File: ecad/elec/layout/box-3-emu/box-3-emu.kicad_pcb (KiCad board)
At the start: 2 copper layers, 72.5 x 63.9 mm, 68 parts

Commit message: feat(ecad): Update ecad / atopile and improve workflow
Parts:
- removed DS1: , lib:SOD-323_L1.8-W1.3-LS2.5-RD
- removed J1: , lib:CONN-SMD_4P-P1.00_SM04B-SRSS-TB-LF-SN
- removed R27: 62.5mW Thick Film Resistors 50V ±100ppm/℃ ±1% 249Ω 0402 Chi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, lib:R0402
- removed U10: , Connector_PinHeader_1.00mm:PinHeader_1x02_P1.00mm_Vertical
- removed U11: , lib:GAMEBOY_COLOR_DPAD_MEMBRANE
- removed U12, U13, U14, U15: , lib:GBC_DPAD_BUTTON
- removed U16, U19: , lib:GAMEBOY_COLOR_A_B_BUTTON_MEMBRANE
- removed U17, U18, U20, U21: , lib:GBC_A_B_BUTTON
- removed U22: , lib:GAMEBOY_COLOR_START_SELECT_MEMBRANE
- removed U23, U24: , lib:GBC_START_SELECT_BUTTON
- removed U25, U26: , lib:SW-SMD_TS24CA
- removed U27: , lib:BOX_3_EMU
- removed U28: , lib:CONN-SMD_5-1734857-1
- removed U7: , lib:DFN-8_L2.0-W2.0-P0.50-BL-EP
- removed U8: , lib:SIM-SMD_C9900007362
- removed U9: , lib:VSSOP-10_L3.0-W3.0-P0.50-LS4.9-BL
- added C10: 22µF ±20%, Samsung_Electro_Mechanics_CL21A226MAQNNNE:C0805, F.Cu at (343.7, -323.6)
- added C11: 22µF ±20%, Samsung_Electro_Mechanics_CL21A226MAQNNNE:C0805, F.Cu at (343.7, -333.6)
- added C12: 100nF ±10%, Samsung_Electro_Mechanics_CL05B104KO5NNNC:C0402, F.Cu at (343.7, -363.6)
- added C13: 100nF ±10%, Samsung_Electro_Mechanics_CL05B104KO5NNNC:C0402, F.Cu at (343.7, -373.6)
- added CN1: , JST_Sales_America_S2B_PH_SM4_TB_LF__SN:CONN-SMD_P2.00_S2B-PH-SM4-TB-LF-SN, B.Cu at (32.4, 24.6)
- added CN2: , JST_Sales_America_SM04B_SRSS_TB_LF__SN:CONN-SMD_4P-P1.00_SM04B-SRSS-TB-LF-SN, F.Cu at (73.7, -33.6)
- added CN3: , TE_Connectivity_5_1734857_1:CONN-SMD_5-1734857-1, F.Cu at (310.0, 0.00)
- added D1: , Guangdong_Hottech_1N5819WS:SOD-323_L1.8-W1.3-LS2.5-RD, F.Cu at (29.6, 17.7)
- added H1: , Ckmtw_B_2100S02P_A110:HDR-TH_2P-P2.54-V-M-1, F.Cu at (44.8, -31.2)
- added MECH1: , GBC_A_B_MEMBRANE:GAMEBOY_COLOR_A_B_BUTTON_MEMBRANE, F.Cu at (64.8, -4.19)
- added MECH2: , GBC_A_B_MEMBRANE:GAMEBOY_COLOR_A_B_BUTTON_MEMBRANE, F.Cu at (59.6, -19.4)
- added MECH3: , GBC_DPAD_MEMBRANE:GAMEBOY_COLOR_DPAD_MEMBRANE, F.Cu at (20.8, -11.8)
- added MECH4: , BOX_EMU_BASE_OUTLINE:BOX_EMU_BASE, F.Cu at (43.7, -33.6)
- added MECH5: , GBC_START_SELECT_MEMBRANE:GAMEBOY_COLOR_START_SELECT_MEMBRANE, F.Cu at (42.2, 10.4)
- added MECH6: , BOX_3_EMU_OUTLINE:BOX_3_EMU, F.Cu at (309.7, -1.05)
- added SW1: , GBC_A_B_BUTTON:GBC_A_B_BUTTON, F.Cu at (71.8, -6.60)
- added SW10: , GBC_START_SELECT_BUTTON:GBC_START_SELECT_BUTTON, F.Cu at (48.4, 10.4)
- added SW11: , SHOU_HAN_TS24CA:SW-SMD_2P-TS24CA, F.Cu at (21.9, 29.1)
- added SW12: , SHOU_HAN_TS24CA:SW-SMD_2P-TS24CA, F.Cu at (27.9, 30.0)
- added SW2: , GBC_A_B_BUTTON:GBC_A_B_BUTTON, F.Cu at (57.9, -1.63)
- added SW3: , GBC_A_B_BUTTON:GBC_A_B_BUTTON, F.Cu at (66.6, -21.9)
- added SW4: , GBC_A_B_BUTTON:GBC_A_B_BUTTON, F.Cu at (52.7, -17.0)
- added SW5: , GBC_DPAD_BUTTON:GBC_DPAD_BUTTON, F.Cu at (20.8, -3.81)
- added SW6: , GBC_DPAD_BUTTON:GBC_DPAD_BUTTON, F.Cu at (12.8, -11.7)
- added SW7: , GBC_DPAD_BUTTON:GBC_DPAD_BUTTON, F.Cu at (28.8, -11.7)
- added SW8: , GBC_DPAD_BUTTON:GBC_DPAD_BUTTON, F.Cu at (20.8, -19.7)
- added SW9: , GBC_START_SELECT_BUTTON:GBC_START_SELECT_BUTTON, F.Cu at (36.8, 10.4)
- added USB1: , Yuandi_TYPE_611_T3_W:USB-C-SMD_TYPE-611-T3-W, F.Cu at (42.5, 30.3)
- C1: value 16V 100nF X7R ±10% 0402 Multilayer Ceramic Capacitors MLCC - SMD/SMT ROHS -> 100nF ±10%; footprint lib:C0402 -> Samsung_Electro_Mechanics_CL05B104KO5NNNC:C0402
- C2: value 25V 10uF X5R ±10% 0805 Multilayer Ceramic Capacitors MLCC - SMD/SMT ROHS -> 1µF ±10%; footprint lib:C0805 -> Samsung_Electro_Mechanics_CL05A105KA5NQNC:C0402
- C3, C4, C5: value 25V 10uF X5R ±10% 0805 Multilayer Ceramic Capacitors MLCC - SMD/SMT ROHS -> 100nF ±10%; footprint lib:C0805 -> Samsung_Electro_Mechanics_CL05B104KO5NNNC:C0402
- C6: value 16V 100nF X7R ±10% 0402 Multilayer Ceramic Capacitors MLCC - SMD/SMT ROHS -> 4.7µF ±10%; footprint lib:C0402 -> Samsung_Electro_Mechanics_CL05A475KP5NRNC:C0402
- C7: value 10V 4.7uF X5R ±20% 0402 Multilayer Ceramic Capacitors MLCC - SMD/SMT ROHS -> 4.7µF ±10%; footprint lib:C0402 -> Samsung_Electro_Mechanics_CL05A475KP5NRNC:C0402
- C8: value 10V 4.7uF X5R ±20% 0402 Multilayer Ceramic Capacitors MLCC - SMD/SMT ROHS -> 10µF ±10%; footprint lib:C0402 -> Samsung_Electro_Mechanics_CL21A106KAYNNNE:C0805
- C9: value 16V 100nF X7R ±10% 0402 Multilayer Ceramic Capacitors MLCC - SMD/SMT ROHS -> 10µF ±10%; footprint lib:C0402 -> Samsung_Electro_Mechanics_CL21A106KAYNNNE:C0805
- L1: footprint lib:IND-SMD_L2.5-W2.0_WPN252012H -> Sunlord_WPN252012H1R5MT:IND-SMD_L2.5-W2.0_WPN252012H
- LED1: footprint lib:LED0805-R-RD -> Yongyu_Photoelectric_SZYY0805R:LED0805-R-RD
- R1, R2: value 62.5mW Thick Film Resistors 50V ±100ppm/℃ ±1% 4.7kΩ 0402 Chip Resistor - Surface Mount ROHS -> 1MΩ ±1%; footprint lib:R0402 -> UNI_ROYAL_0402WGF1004TCE:R0402
- R10: value 62.5mW Thick Film Resistors 50V ±100ppm/℃ ±1% 2kΩ 0402 Chip Resistor - Surface Mount ROHS -> 10kΩ ±1%; footprint lib:R0402 -> UNI_ROYAL_0402WGF1002TCE:R0402
- R11: value 62.5mW Thick Film Resistors 50V ±100ppm/℃ ±1% 2.55kΩ 0402 Chip Resistor - Surface Mount ROHS -> 10kΩ ±1%; footprint lib:R0402 -> UNI_ROYAL_0402WGF1002TCE:R0402
- R12, R13, R14, R15, R16, R18, R19, R20, R25, R3, R4, R5, R6: value 62.5mW Thick Film Resistors 50V ±100ppm/℃ ±1% 10kΩ 0402 Chip Resistor - Surface Mount ROHS -> 10kΩ ±1%; footprint lib:R0402 -> UNI_ROYAL_0402WGF1002TCE:R0402
- R17, R23, R24: value 62.5mW Thick Film Resistors 50V ±100ppm/℃ ±1% 10kΩ 0402 Chip Resistor - Surface Mount ROHS -> 5.1kΩ ±1%; footprint lib:R0402 -> UNI_ROYAL_0402WGF5101TCE:R0402
- R21: value 62.5mW Thick Film Resistors 50V ±100ppm/℃ ±1% 10kΩ 0402 Chip Resistor - Surface Mount ROHS -> 91kΩ ±1%; footprint lib:R0402 -> YAGEO_RC0402FR_0791KL:R0402
- R22: value 62.5mW Thick Film Resistors 50V ±100ppm/℃ ±1% 10kΩ 0402 Chip Resistor - Surface Mount ROHS -> 820kΩ ±1%; footprint lib:R0402 -> FOJAN_FRC0402F8203TS:R0402
- R26: value 62.5mW Thick Film Resistors 50V ±100ppm/℃ ±1% 255Ω 0402 Chip Resistor - Surface Mount ROHS -> 10kΩ ±1%; footprint lib:R0402 -> UNI_ROYAL_0402WGF1002TCE:R0402
- R7: value 62.5mW Thick Film Resistors ±100ppm/℃ ±1% 243kΩ 0402 Chip Resistor - Surface Mount ROHS -> 2kΩ ±1%; footprint lib:R0402 -> UNI_ROYAL_0402WGF2001TCE:R0402
- R8: value 62.5mW Thick Film Resistors 50V ±100ppm/℃ ±1% 27.4kΩ 0402 Chip Resistor - Surface Mount ROHS -> 10kΩ ±1%; footprint lib:R0402 -> UNI_ROYAL_0402WGF1002TCE:R0402
- R9: value 62.5mW Thick Film Resistors 50V ±100ppm/℃ ±1% 1MΩ 0402 Chip Resistor - Surface Mount ROHS -> 10kΩ ±1%; footprint lib:R0402 -> UNI_ROYAL_0402WGF1002TCE:R0402
- U1: footprint lib:BOX_EMU_BASE -> Texas_Instruments_DRV2605LDGSR:VSSOP-10_L3.0-W3.0-P0.50-LS4.9-BL
- U2: footprint lib:CONN-SMD_P2.00_S2B-PH-SM4-TB-LF-SN -> AWINIC_AW9523BTQR:VFQFPN-24_L4.0-W4.0-P0.50-BL-EP2.8; moved to F.Cu
- U3: footprint lib:USB-C-SMD_TYPE-611-T3-W -> Maxim_Integrated_MAX17048G_T10:TDFN-8_L2.0-W2.0-P0.50-BL-EP1.2
- U4: footprint lib:VFQFPN-24_L4.0-W4.0-P0.50-BL-EP2.8 -> Microchip_Tech_MCP73831T_2ACI_OT:SOT-23-5_L3.0-W1.7-P0.95-LS2.8-BL
- U5: footprint lib:VSON-14_L4.0-W3.0-P0.50-BL-EP_TI_DSJ -> Texas_Instruments_TPS63020DSJR:VSON-14_L4.0-W3.0-P0.50-BL-EP_TI_DSJ
- U6: footprint lib:SOT-23-5_L3.0-W1.7-P0.95-LS2.8-BL -> HOAUC_HYCW118_TF09_200B:SIM-SMD_C9900007362
- moved R25 568.7 mm to (343.7, -403.6), turned to 0 degrees
- moved R26 565.8 mm to (343.7, -413.6), turned to 0 degrees
- moved R24 559.1 mm to (343.7, -393.6), turned to 0 degrees
- moved R23 529.3 mm to (343.7, -383.6), turned to 0 degrees
- moved R22 497.8 mm to (343.7, -353.6)
- moved C9 481.7 mm to (343.7, -313.6), turned to 0 degrees
- moved C8 471.9 mm to (343.7, -303.6), turned to 0 degrees
- moved R21 455.4 mm to (343.7, -343.6), turned to 0 degrees
- moved C6 444.4 mm to (343.7, -273.6), turned to 0 degrees
- moved C7 436.2 mm to (343.7, -263.6), turned to 0 degrees
- moved C5 432.4 mm to (343.7, -253.6), turned to 0 degrees
- moved R18 391.1 mm to (343.7, -243.6), turned to 0 degrees
- moved C4 390.5 mm to (343.7, -203.6), turned to 0 degrees
- moved R17 380.4 mm to (343.7, -233.6), turned to 0 degrees
- moved R16 375.7 mm to (343.7, -223.6), turned to 0 degrees
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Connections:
- net l1 renamed 1
- net l2 renamed 2
- C1 pad 1: vcc_3v3 -> battery_measurement
- C1 pad 2: box-gnd -> gnd
- C2 pad 1: vbat -> hv
- C2 pad 2: box-gnd -> gnd
- C3 pad 1: vbat -> vcc_3v3
- C3 pad 2: box-gnd -> gnd
- C4 pad 1: vcc_5v -> vcc_3v3
- C4 pad 2: box-gnd -> gnd
- C5 pad 1: vcc_5v -> vbat
- C5 pad 2: box-gnd -> gnd
- C6 pad 1: vina -> vbat
- C6 pad 2: box-gnd -> gnd
- C7 pad 2: box-gnd -> gnd
- C8 pad 2: box-gnd -> gnd
- C9 pad 2: box-gnd -> gnd
- LED1 pad 1: vbus -> pos
- LED1 pad 2: cathode -> STAT
- R1 pad 1: cc1 -> battery_measurement
- R1 pad 2: box-gnd -> gnd
- R10 pad 1: prog -> vcc_3v3
- R10 pad 2: box-gnd -> right
- R11 pad 1: cathode -> vcc_3v3
- R11 pad 2: box.mcp73831-gnd -> up
- R12 pad 1: p1_3 -> EN
- R13 pad 1: en -> vcc_3v3
- R13 pad 2: vcc_3v3 -> SCL
- R14 pad 2: up -> SDA
- R15 pad 2: down -> INTN
- R16 pad 2: left -> RSTN
- R17 pad 1: vcc_3v3 -> vbus
- R17 pad 2: right -> pos
- R18 pad 1: vcc_3v3 -> nALRT
- R18 pad 2: box.io-a -> vcc_3v3
- R19 pad 2: box.io-b -> select
- R2 pad 1: cc2 -> vbat
- R2 pad 2: box-gnd -> battery_measurement
- R20 pad 2: x -> start
- R21 pad 1: vcc_3v3 -> FB
- R21 pad 2: y -> gnd
- R22 pad 1: vcc_3v3 -> vcc_5v
- R22 pad 2: start -> FB
- R23 pad 1: vcc_3v3 -> A5
- R23 pad 2: select -> gnd
- R24 pad 1: vcc_3v3 -> B5
- R24 pad 2: vol_up -> gnd
- R26 pad 1: vbat -> vcc_3v3
- R26 pad 2: battery_measurement -> vol_up
- R3 pad 1: sda -> vcc_3v3
- R3 pad 2: vcc_3v3 -> line
- R4 pad 1: scl -> vcc_3v3
- R4 pad 2: vcc_3v3 -> buttons_abxy-b-line
- R5 pad 2: rstn -> x_y_btns-a-line
- R6 pad 2: intn -> x_y_btns-b-line
- R7 pad 1: vcc_5v -> PROG
- R7 pad 2: out -> gnd
- R8 pad 1: out -> vcc_3v3
- R8 pad 2: box-gnd -> down
- R9 pad 1: pg -> vcc_3v3
- R9 pad 2: box-gnd -> left
- U2 pad 1: vbat -> start
- U2 pad 2: box-gnd -> select
- U2 pad 3: box-gnd -> 3
- U2 pad 4: box-gnd -> nALRT
- U4 pad 1: start -> STAT
- U4 pad 2: select -> gnd
- U4 pad 3: p1_2 -> vbat
- U4 pad 4: p1_3 -> vbus
- U4 pad 5: up -> PROG
- U5 pad 1: vina -> vbat
- U5 pad 12: vina -> vbat
- U5 pad 13: box-gnd -> gnd
- U5 pad 14: pg -> PG
- U5 pad 15: box-gnd -> gnd
- U5 pad 2: box-gnd -> gnd
- U5 pad 3: out -> FB
- U6 pad 1: box.mcp73831-gnd -> box.uSD.card-1
- U6 pad 2: box-gnd -> io10
- U6 pad 3: vbat -> MOSI
- U6 pad 4: vbus -> vcc_3v3
- U6 pad 5: prog -> SCLK
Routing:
- net box-gnd: track 489.4 -> 0.00 mm, vias 14 -> 0
- net vcc_3v3: track 169.2 -> 0.00 mm, vias 17 -> 0
- net sda: track 144.1 -> 0.00 mm, vias 7 -> 0
- net miso: track 136.8 -> 0.00 mm, vias 2 -> 0
- net scl: track 136.3 -> 0.00 mm, vias 4 -> 0
- net dp: track 133.0 -> 0.00 mm, vias 1 -> 0
- net sck: track 130.0 -> 0.00 mm, vias 1 -> 0
- net mosi: track 118.5 -> 0.00 mm, vias 1 -> 0
- net cs: track 114.0 -> 0.00 mm, vias 2 -> 0
- net dm: track 80.5 -> 0.00 mm, vias 1 -> 0
- net box.io-b: track 77.7 -> 0.00 mm
- net down: track 69.4 -> 0.00 mm, vias 2 -> 0
- net vbus: track 68.5 -> 0.00 mm, vias 4 -> 0
- net battery_measurement: track 63.4 -> 0.00 mm, vias 2 -> 0
- net y: track 63.1 -> 0.00 mm
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- removed copper zone on F.Cu, net box-gnd
- removed copper zone on B.Cu, net vcc_3v3
- removed copper zone on B.Cu, net vcc_5v
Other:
- board text removed: "A"
- board text removed: "B"
- board text removed: "DOWN"
- board text removed: "LEFT"
- board text removed: "RIGHT"
- board text removed: "SELECT"
- board text removed: "START"
- board text removed: "UP"
- board text removed: "X"
- board text removed: "Y"

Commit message: improve workflow
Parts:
- moved MECH6 269.8 mm to (42.2, -36.1)
- moved CN3 269.5 mm to (42.9, -35.4), turned to 180 degrees
- moved U6 11.4 mm to (56.9, 24.5), turned to 6 degrees
- moved USB1 1.54 mm to (42.5, 28.7)
- moved CN1 0.46 mm to (32.7, 25.0), turned to 0 degrees
- turned SW11 to 170 degrees
- turned SW12 to 174 degrees
- turned SW3 to 180 degrees
- turned SW4 to 180 degrees
- turned SW5 to 90 degrees
- turned SW7 to 180 degrees
- turned SW8 to 270 degrees

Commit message: improve placement of components and robustness of scripts
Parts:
- MECH1, MECH2: value (none) -> SILKSCREENGBC_A/B
- REF**: renamed from MECH4; value (none) -> BOX_EMU_BASE
- U$1: renamed from MECH3; value (none) -> SILKSCREENGBC_D-PAD
- U$2: renamed from MECH5; value (none) -> SILKSCREENGBC_START/SELECT
- moved R24 563.6 mm to (148.2, 135.0), turned to 180 degrees
- moved R26 560.0 mm to (146.6, 110.5), turned to 180 degrees
- moved R23 555.4 mm to (148.2, 136.2), turned to 180 degrees
- moved R25 549.5 mm to (146.6, 109.4), turned to 180 degrees
- moved C12 533.7 mm to (97.5, 109.9)
- moved C13 533.7 mm to (97.5, 99.9)
- moved R22 528.4 mm to (130.4, 129.9), turned to 180 degrees
- moved R21 518.2 mm to (130.4, 128.7), turned to 180 degrees
- moved C11 504.1 mm to (135.2, 125.4), turned to 90 degrees
- moved C9 491.3 mm to (136.1, 131.7), turned to 180 degrees
- moved C8 481.3 mm to (125.9, 125.6), turned to 90 degrees
- moved C10 456.9 mm to (137.2, 83.9), turned to 90 degrees
- moved C5 434.5 mm to (105.9, 110.0)
- moved C6 434.5 mm to (105.9, 90.0)
- moved C7 434.5 mm to (105.9, 100.0)
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- renumbered MECH6 to U1, SW1 to U2, SW2 to U2, SW4 to U2, SW3 to U2, SW9 to U3, SW10 to U3, SW7 to U5, SW5 to U5, SW8 to U5, SW6 to U5

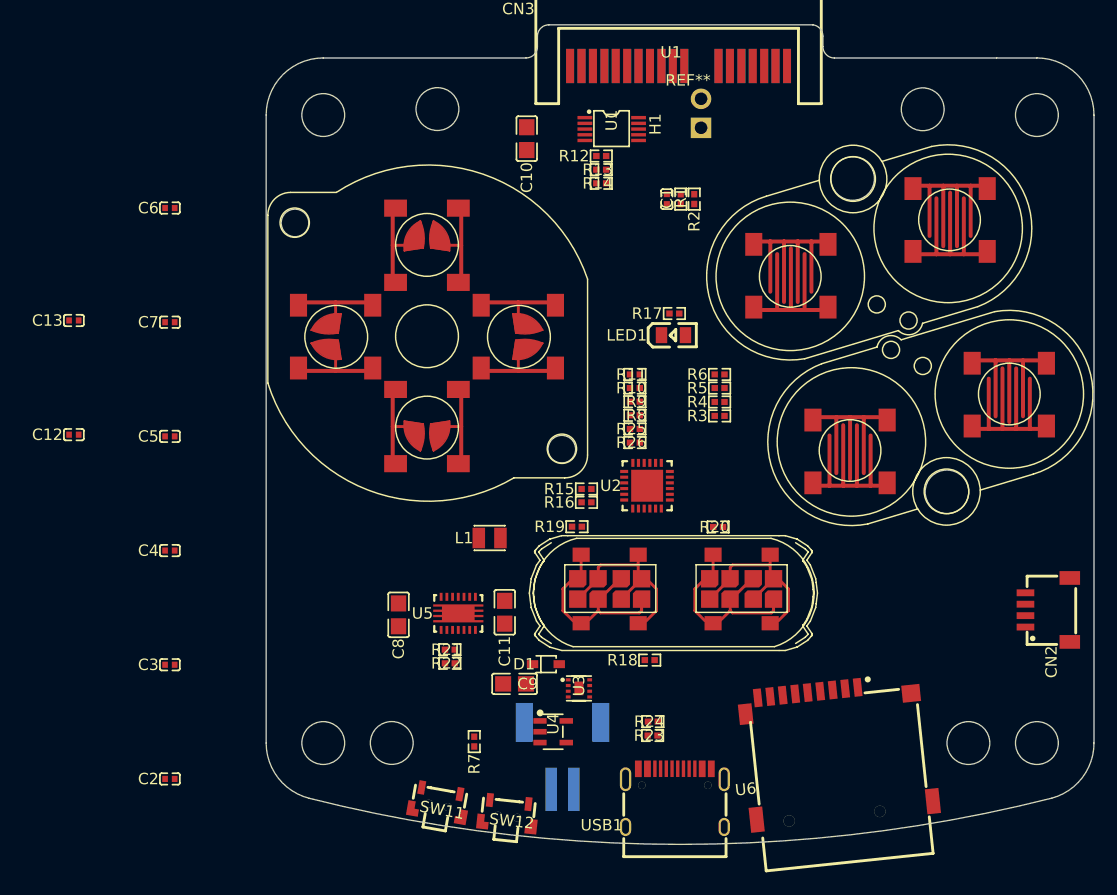
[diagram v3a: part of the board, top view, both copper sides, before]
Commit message: nudge layouts some
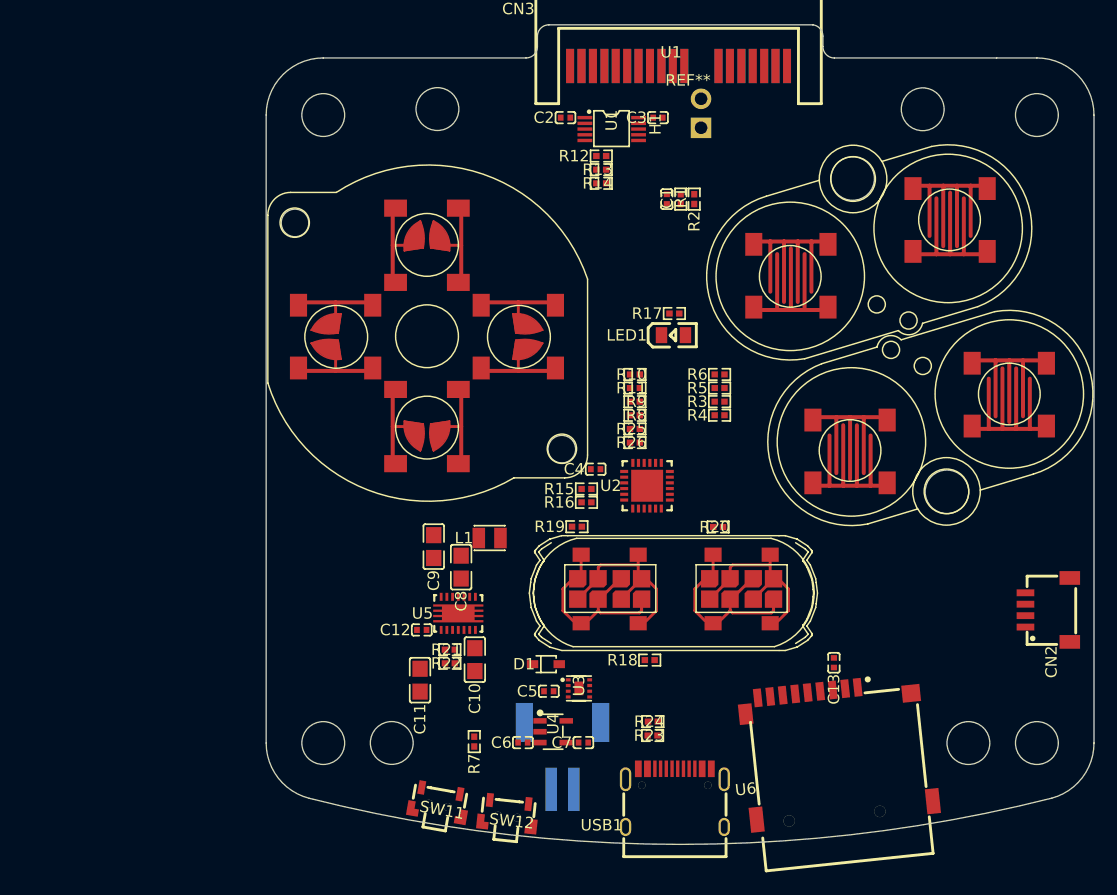
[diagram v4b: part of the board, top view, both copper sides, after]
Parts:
- moved C13 73.0 mm to (164.1, 129.8), turned to 90 degrees
- moved C2 67.5 mm to (140.6, 82.1)
- moved C3 64.2 mm to (148.7, 82.1)
- moved C6 56.1 mm to (136.8, 136.8)
- moved C7 51.6 mm to (142.1, 136.8)
- moved C10 45.9 mm to (132.6, 129.6)
- moved C5 40.0 mm to (139.1, 132.3)
- moved C4 38.0 mm to (143.2, 112.9)
- moved C12 34.9 mm to (128.0, 127.0)
- moved C9 14.0 mm to (129.0, 119.7), turned to 90 degrees
- moved C11 9.51 mm to (127.8, 131.4)
- moved C8 6.89 mm to (131.4, 121.5)
- moved R3 1.25 mm to (154.1, 107.0)
- moved R11 1.19 mm to (146.6, 105.8)
- moved R10 1.19 mm to (146.6, 104.6)
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
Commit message: further layout changes
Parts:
- moved L1 6.66 mm to (134.8, 125.5), turned to 270 degrees
- moved C11 3.45 mm to (131.3, 131.4), turned to 180 degrees
- moved R22 2.15 mm to (128.6, 128.8)
- moved R21 2.14 mm to (128.6, 129.7), turned to 0 degrees
- moved C9 2.04 mm to (130.9, 120.5), turned to 180 degrees
- moved C10 1.36 mm to (131.3, 129.6), turned to 180 degrees
- moved C8 1.02 mm to (130.9, 122.3), turned to 180 degrees
- turned C12 to 180 degrees
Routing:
- net gnd: track 0.00 -> 21.5 mm
- net vcc_5v: track 0.00 -> 11.1 mm
- net vbat: track 0.00 -> 7.45 mm
- net FB: track 0.00 -> 5.30 mm
- net 2: track 0.00 -> 3.15 mm
- net 1: track 0.00 -> 3.15 mm

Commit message: fixing some issues
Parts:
- MECH1, MECH2: value SILKSCREENGBC_A/B -> (none)
- REF**: value BOX_EMU_BASE -> (none)
- U$1: value SILKSCREENGBC_D-PAD -> (none)
- U$2: value SILKSCREENGBC_START/SELECT -> (none)
- renumbered U1 to MECH3, U2 to SW1, U3 to SW10, U2 to SW2, U2 to SW3, U2 to SW4, U5 to SW5, U5 to SW6, U5 to SW7, U5 to SW8, U3 to SW9
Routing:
- net gnd: track 21.5 -> 3.71 mm
- net vcc_5v: track 11.1 -> 4.03 mm
- net 2: track 3.15 -> 0.00 mm
- net 1: track 3.15 -> 0.00 mm
- net vbat: track 7.45 -> 5.69 mm, vias 0 -> 2
- added copper zone on F.Cu, net 1
- added copper zone on F.Cu, net 2
- added copper zone on F.Cu, net gnd
- added copper zone on F.Cu, net vbat
- added copper zone on F.Cu, net vcc_5v
